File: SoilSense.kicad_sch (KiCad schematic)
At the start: 22 parts, among them J3 OSTVN04A150, Q5 PMH950UPEH, U4 SN75176BDR, U8 74HC04D

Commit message: 2nd rev schematic done
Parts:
- removed C12: 100nF, Capacitor_SMD:C_0402_1005Metric, symbol Device:C_Small
- removed D9: 1N4148WS, Diode_SMD:D_SOD-323, symbol Diode:1N4148WS
- removed Q5: PMH950UPEH, SproutSenseFootprints:QPMOS1G2S3d_SOT8001_NEX, symbol SproutSense:PMH950UPEH
- removed R14: 22k, Resistor_SMD:R_0402_1005Metric, symbol Device:R_Small_US
- removed U4: SN75176BDR, Package_SO:SOP-8_3.76x4.96mm_P1.27mm, symbol SproutSense:SN75176BDR
- removed U8: 74HC04D, Package_SO:SOIC-14_3.9x8.7mm_P1.27mm, symbol SproutSense:74HC04D
- added C13, C14: 1uF, Capacitor_SMD:C_0402_1005Metric, symbol Device:C_Small
- added Q5: SIUD412ED-T1-GE3, SMT_412ED-T1-GE3_VIS, symbol SproutSense:SIUD412ED-T1-GE3
- added R18: 4.7k, Resistor_SMD:R_0402_1005Metric, symbol Device:R_Small_US
- added TP4, TP5, TP6, TP7, TP8: TestPoint, symbol Connector:TestPoint
- added U10: TXB0104DR, SproutSenseFootprints:SOIC127P600X175-14N, symbol SproutSense:TXB0104DR
- added U4: SN65HVD3082EDR, SproutSenseFootprints:SOIC127P599X175-8N, symbol SproutSense:SN65HVD3082EDR
- C8: value 100nF -> 1uF; Distributor Prt # 1276-1002-1-ND -> 490-10024-1-ND - Cut Tape (CT); Manuf Prt # CL05B104KP5NNNC -> GRM155R70J105KA12D
- R2, R6: value 4.7k -> 1k; Distributor Prt # 311-4.7KJRCT-ND -> 311-1.0KJRCT-ND; Manuf Prt # RC0402JR-074K7L -> RC0402JR-071KL
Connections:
- net +5V: now also J3.1 (Pin_1), C14.1, U10.14 (VCCB), U4.8 (VCC); no longer R1.2
- net GND: now also R1.1, C13.2, C14.2, Q5.2 (S), R18.2, U10.7 (GND), U4.5 (GND); no longer J3.4 (Pin_4)
- net RE/DE: now also U10.11 (B3), U4.2 (~{RE}), U4.3 (DE)
- net RS485_A+: now also D1.2 (A2), D2.1 (A1), R3.1, R4.1, TP4.1, U4.6 (A); no longer D1.1 (A1), D3.2 (A2), R3.2, R5.2, TP2.1
- net RS485_B-: now also D1.1 (A1), D3.2 (A2), R3.2, R5.2, TP3.1, U4.7 (B); no longer D1.2 (A2), D2.1 (A1), R3.1, R4.1, TP1.1
- net RX: now also U10.12 (B2), U4.1 (R)
- net SOIL_SNS_ENA: now also R1.2, Q5.1 (G), TP8.1; no longer R1.1
- net TX: now also U10.13 (B1), U4.4 (D)
- net UART_RX: now also TP1.1, U10.3 (A2)
- net UART_TX: now also TP2.1, U10.2 (A1)
- net WRT_ENA: now also TP6.1, U10.4 (A3); no longer TP3.1
- new net +3V3: C13.1, U10.1 (VCCA)
- new net GND1: J3.4 (Pin_4), Q5.3 (D), TP5.1
- new net SERIAL_OE: R18.1, TP7.1, U10.8 (OE)
- no-connect marks 0 -> 2
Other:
- note added: "Low Side Switch for controlling ground connection to soil sensors"
- note removed: "Diode acts as half rectifier RC TimeConstant needs to be adequate to remain high between bit writes Tuned for baud rate of 4800/9600"
- note removed: "TC = R14 * C12 = 22k * 100n = 2.2ms"
- moved on the sheet: D1, D2, D3, D4, D5, J3, R3, R4, R5

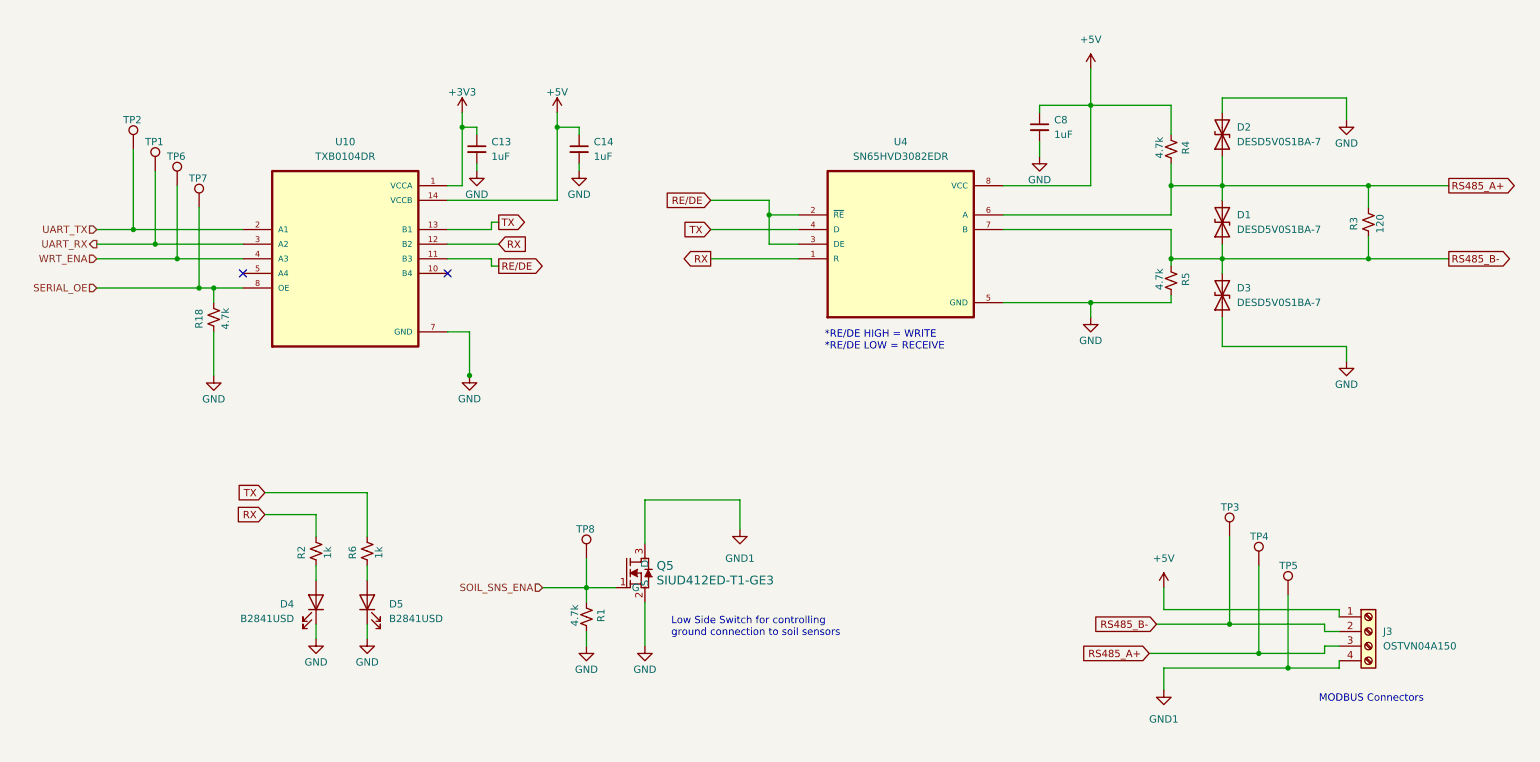
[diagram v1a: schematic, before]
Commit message: mostly routed
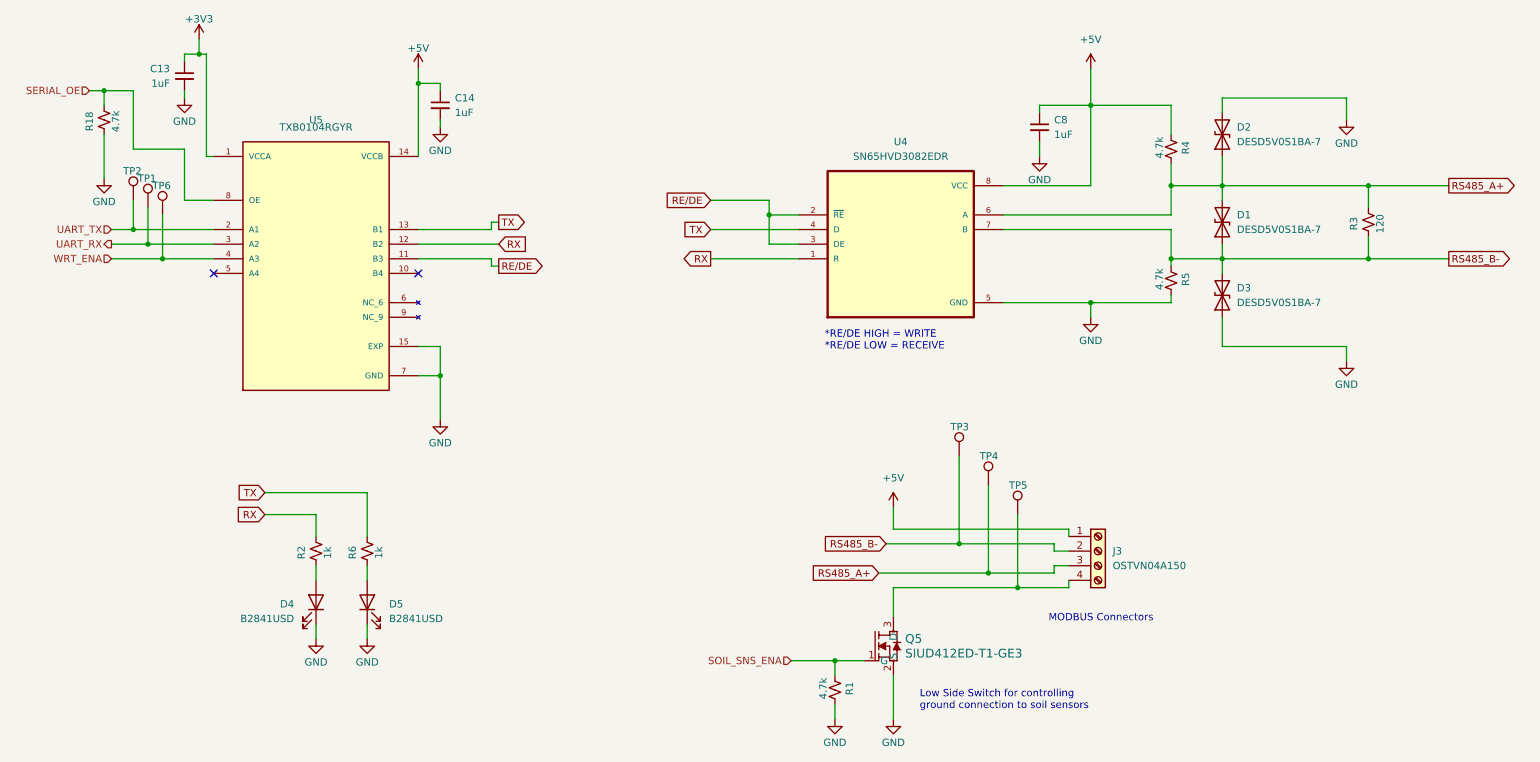
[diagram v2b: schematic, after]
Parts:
- removed TP7, TP8: TestPoint, symbol Connector:TestPoint
- removed U10: TXB0104DR, SproutSenseFootprints:SOIC127P600X175-14N, symbol SproutSense:TXB0104DR
- added U5: TXB0104RGYR, SproutSenseFootprints:QFN50P350X350X100-15N, symbol SproutSense:TXB0104RGYR
- Q5: Distributor Prt # (none) -> SIUD412ED-T1-GE3CT-ND; Manuf Prt # (none) -> SIUD412ED-T1-GE3
- TP1, TP2, TP3, TP4, TP5, TP6: footprint (none) -> TestPoint:TestPoint_Pad_D1.0mm
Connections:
- net +3V3: now also U5.1 (VCCA)
- net +5V: now also U5.14 (VCCB)
- net GND: now also U5.15 (EXP), U5.7 (GND)
- net RE/DE: now also U5.11 (B3)
- net RX: now also U5.12 (B2)
- net SERIAL_OE: now also U5.8 (OE)
- net TX: now also U5.13 (B1)
- net UART_RX: now also U5.3 (A2)
- net UART_TX: now also U5.2 (A1)
- net WRT_ENA: now also U5.4 (A3)
- net GND1: no longer names the net of J3.4 (Pin_4), Q5.3 (D), TP5.1
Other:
- moved on the sheet: C13, C14, J3, Q5, R1, R18, TP1, TP2, TP3, TP4, TP5, TP6

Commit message: Removed via in pads
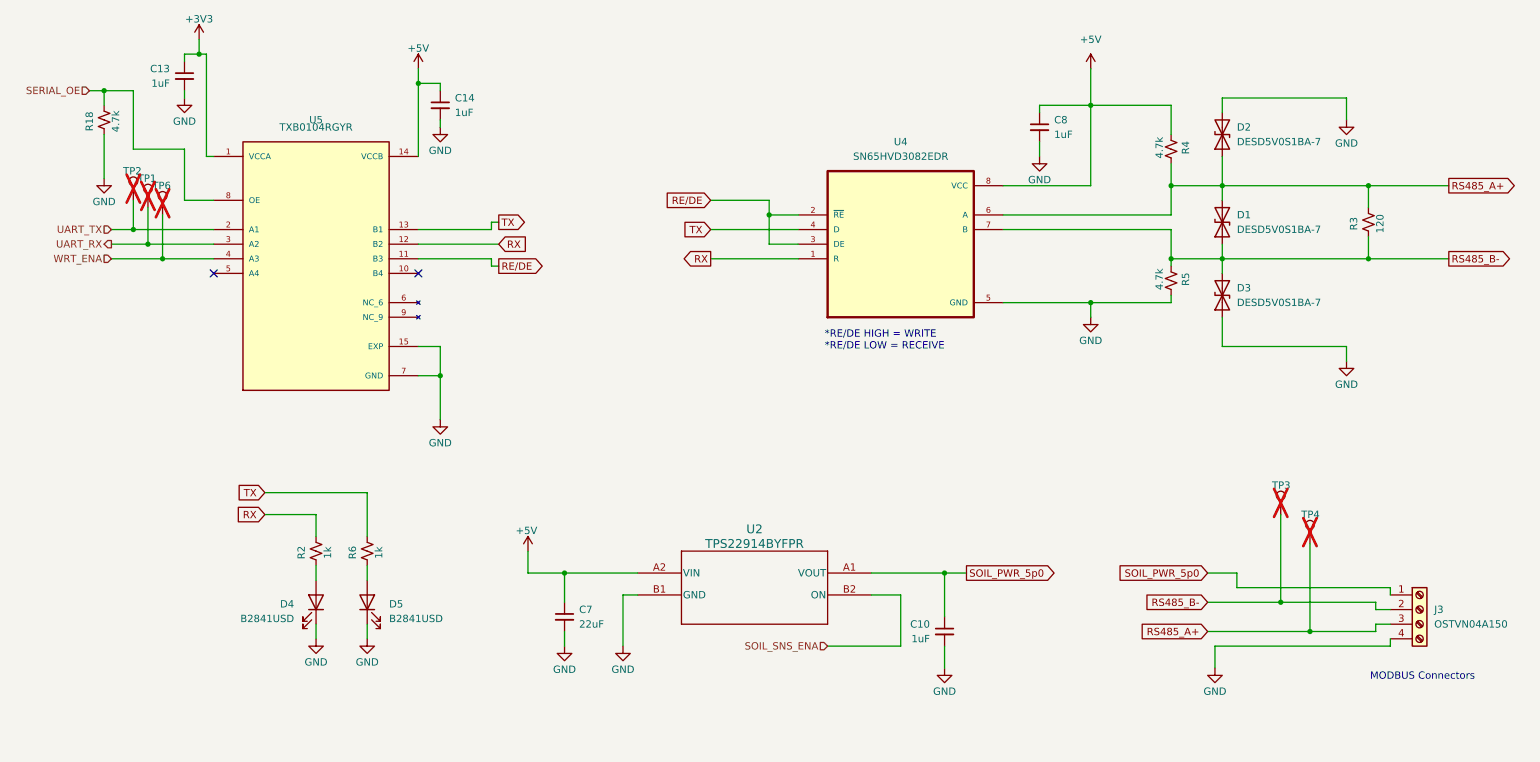
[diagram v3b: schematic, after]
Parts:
- removed Q5: SIUD412ED-T1-GE3, SMT_412ED-T1-GE3_VIS, symbol SproutSense:SIUD412ED-T1-GE3
- removed R1: 4.7k, Resistor_SMD:R_0402_1005Metric, symbol Device:R_Small_US
- removed TP5: TestPoint, TestPoint:TestPoint_Pad_D1.0mm, symbol Connector:TestPoint
- added C10: 1uF, Capacitor_SMD:C_0402_1005Metric, symbol Device:C_Small
- added C7: 22uF, Capacitor_SMD:C_0402_1005Metric, symbol Device:C_Small
- added U2: TPS22914BYFPR, SproutSenseFootprints:YFP4_TEX, symbol SproutSense:TPS22914BYFPR
- TP1, TP2, TP3, TP4, TP6: now not fitted
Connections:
- net +5V: now also C7.1, U2.A2 (VIN); no longer J3.1 (Pin_1)
- net GND: now also J3.4 (Pin_4), C10.2, C7.2, U2.B1 (GND)
- net SOIL_SNS_ENA: now also U2.B2 (ON)
- new net SOIL_PWR_5p0: C10.1, J3.1 (Pin_1), U2.A1 (VOUT)
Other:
- note removed: "Low Side Switch for controlling ground connection to soil sensors"
- moved on the sheet: J3
